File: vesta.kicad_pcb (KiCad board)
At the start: 2 copper layers, 39 parts, among them J1 Solar Panel, J2 Solar Panel, J4 Conn_02x07_Odd_Even, U2 BQ24074RGTR, U3 TPS63900DSKR, U4 BME688_C3664478, U5 RAK3172-T-8-SM-I

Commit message: feat: PCB design ready
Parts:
- added G***: LOGO, Logo:logo, F.Cu at (54.3, 77.0)
- moved BATTERY1 56.7 mm to (44.5, 22.7), turned to 180 degrees
- moved U4 55.2 mm to (44.9, 78.8)
- moved C22 54.8 mm to (42.2, 77.2)
- moved C23 54.7 mm to (42.2, 79.2)
- moved J1 44.7 mm to (53.0, 30.7), turned to 180 degrees
- moved J2 42.7 mm to (36.5, 30.7), turned to 180 degrees
- moved R16 39.8 mm to (57.8, 68.0), turned to 90 degrees
- moved R15 39.1 mm to (56.2, 68.0), turned to 90 degrees
- moved TP2 37.1 mm to (60.5, 67.0), turned to 180 degrees
- moved D1 35.6 mm to (47.0, 33.5), turned to -90 degrees
- moved C2 33.1 mm to (42.5, 34.5), turned to -90 degrees
- moved C1 33.0 mm to (44.5, 34.5), turned to -90 degrees
- moved TP1 32.7 mm to (56.8, 43.0), turned to 180 degrees
- moved TP3 30.0 mm to (35.2, 61.2)
- moved R11 29.5 mm to (35.2, 63.2)
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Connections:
- U5 pad 2: unconnected-(U5-PA2/UART2_TX-Pad2) -> /UART_TX
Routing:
- net /3V3_SYS: track 5.55 -> 106.5 mm
- net /I2C1_SCL: track 0.00 -> 55.6 mm, vias 0 -> 1
- net /I2C1_SDA: track 0.00 -> 53.2 mm, vias 0 -> 1
- net /VIN_SOLAR: track 0.00 -> 43.9 mm, vias 0 -> 1
- net /NRST: track 0.00 -> 31.5 mm, vias 0 -> 2
- net /BAT_RAW: track 0.00 -> 28.2 mm
- net /SYS_RAW: track 0.00 -> 28.1 mm, vias 0 -> 2
- net GND: track 0.00 -> 26.2 mm, vias 0 -> 4
- net /EXP_SPI_CS0: track 0.00 -> 25.1 mm, vias 0 -> 1
- net /SWO: track 0.00 -> 24.6 mm, vias 0 -> 2
- net /EXP_GPIO_CS1: track 0.00 -> 20.5 mm
- net /SPI1_MOSI: track 0.00 -> 20.0 mm
- net /SPI1_MISO: track 0.00 -> 18.0 mm
- net /EXP_INT_WAKE: track 0.00 -> 16.4 mm, vias 0 -> 1
- net /SPI1_SCK: track 0.00 -> 16.1 mm
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- added copper zone on B.Cu, net GND
- added copper zone on F.Cu, net GND
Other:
- board outline added: 41 x 60.2 mm
- board text added: "()()()()() ()()()()()()() ()()()()()()()()() ()()()()()()()()() ()()()()()()()()()()() ()()()()()()()()()()() ()()()()()()()()()()()() ()()()()()()()()()()()()() ()()()()()()()()()()()()()() ()()()()()()()()()()()()()()() ()()()()()()()()()()()()()()()() ()()()()()()()()()()()()()()()()() ()()()()()()()()()()()()()()()()() ()()()()()()()()()()()()()()()()() ()()()()()()()()()()()()()()()()() ()()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"
- board text added: "3V3"
- board text added: "EXP GPIO CS1"
- board text added: "EXP SPI CS0"
- board text added: "EXP_INT WAKE"
- board text added: "GND"
- board text added: "I2C1 SCL"
- board text added: "I2C1 SDA"
- board text added: "SPI1 MISO"
- board text added: "SPI1 MOSI"
- board text added: "SPI1 SCK"
- board text added: "Vesta Golden Marina Industries"
- board text removed: "()()() ()()()()() ()()()()()()() ()()()()()()()() ()()()()()()()()()()() ()()()()()()()()()()() ()()()()()()()()()()()() ()()()()()()()()()()()()() ()()()()()()()()()()()()()() ()()()()()()()()()()()()()()() ()()()()()()()()()()()()()()()() ()()()()()()()()()()()()()()()()() ()()()()()()()()()()()()()()()()() ()()()()()()()()()()()()()()()()() ()()()()()()()()()()()()()()()()() ()()()()()()()()()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"

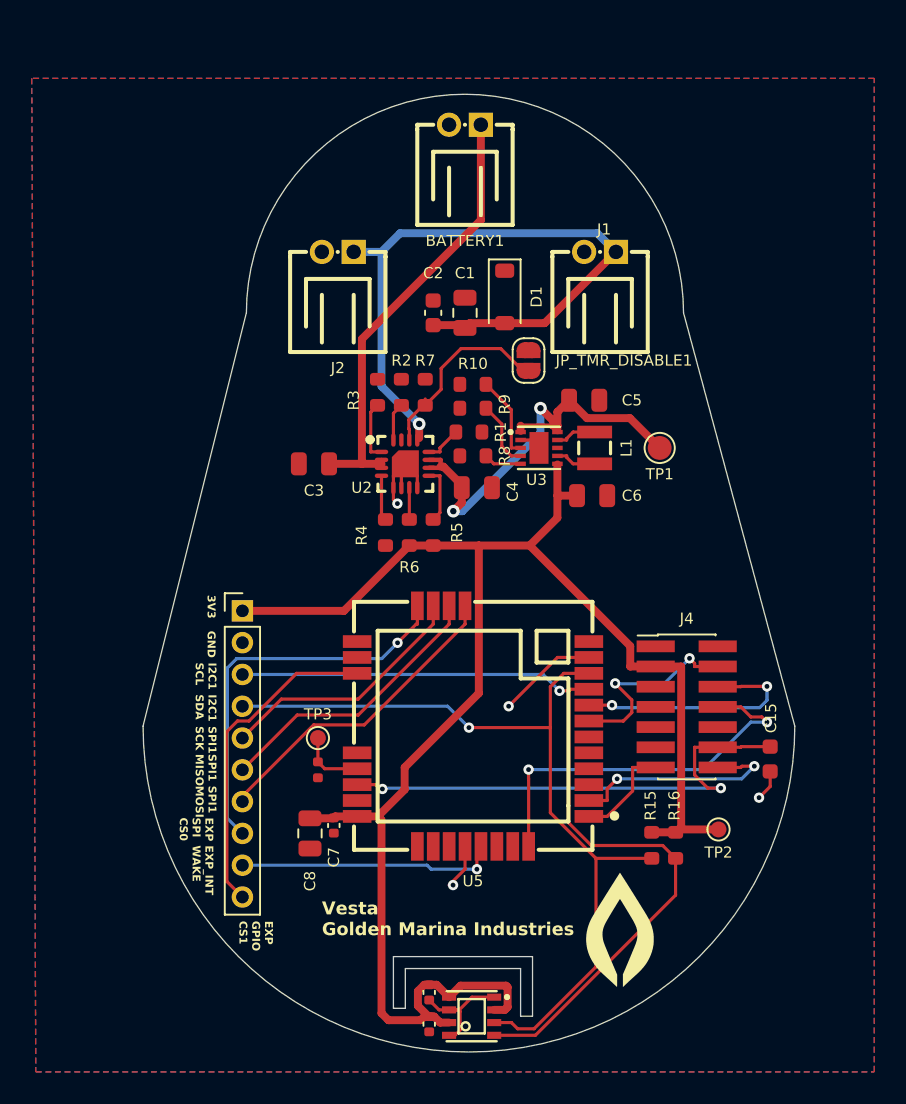
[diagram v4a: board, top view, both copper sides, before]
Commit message: feat: updaing the BOM and adding the STLINK connector
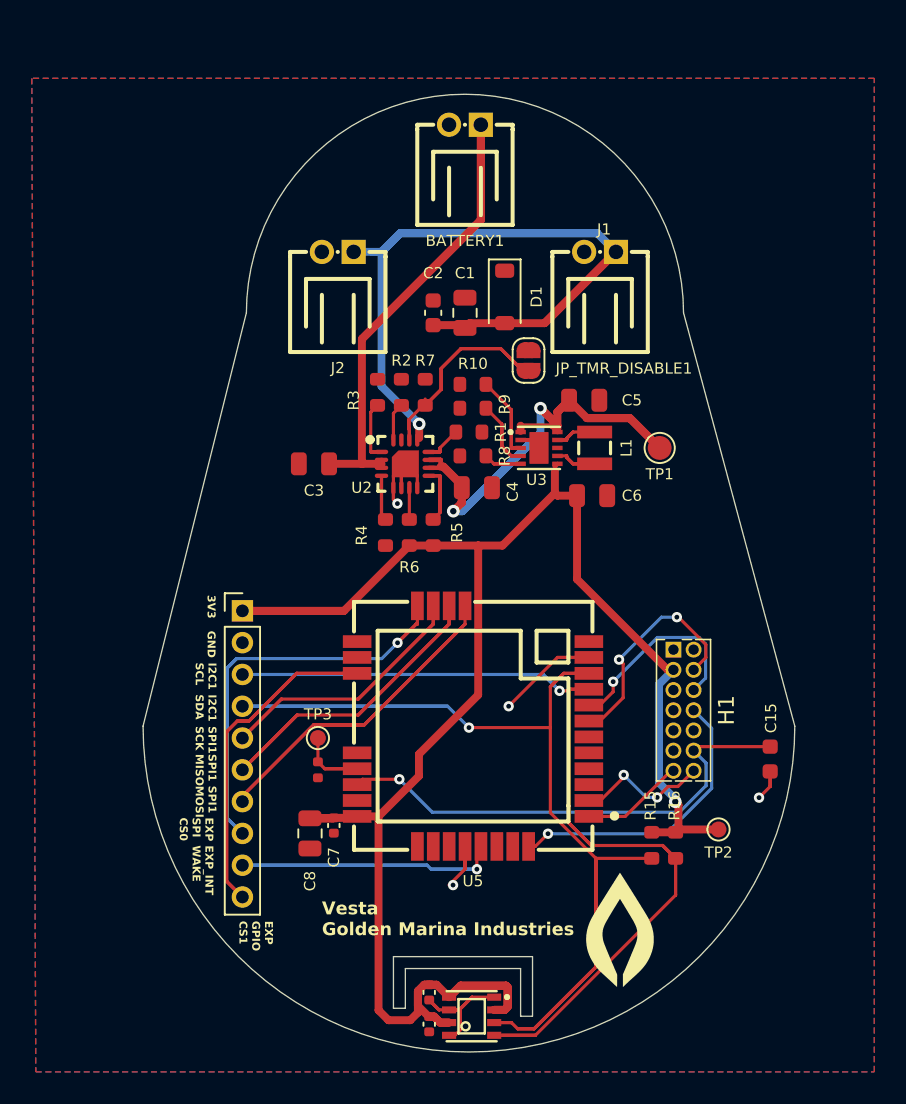
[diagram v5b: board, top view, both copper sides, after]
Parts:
- removed J4: Conn_02x07_Odd_Even, Connector_PinHeader_1.27mm:PinHeader_2x07_P1.27mm_Vertical_SMD
- added H1: HX_PZ1_27-2X7P_ZZ, JLCImport:HX_PZ1_27-2X7P_ZZ, F.Cu at (58.2, 59.5)
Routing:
- net /I2C1_SDA: track 53.2 -> 83.3 mm
- net /VIN_SOLAR: track 43.9 -> 65.5 mm
- net /I2C1_SCL: track 55.6 -> 74.6 mm
- net /SPI1_MOSI: track 20.0 -> 38.8 mm
- net /SYS_RAW: track 28.1 -> 46.7 mm
- net /3V3_SYS: track 106.5 -> 123.7 mm, vias 0 -> 1
- net /BAT_RAW: track 28.2 -> 44.8 mm
- net /EXP_INT_WAKE: track 16.4 -> 30.9 mm
- net GND: track 26.2 -> 40.6 mm
- net /SPI1_MISO: track 18.0 -> 32.1 mm
- net /EXP_SPI_CS0: track 25.1 -> 38.4 mm
- net /SPI1_SCK: track 16.1 -> 27.4 mm
- net /EXP_GPIO_CS1: track 20.5 -> 31.6 mm
- net Net-(JP_TMR_DISABLE1-A): track 12.4 -> 22.8 mm
- net /SWO: track 24.6 -> 18.4 mm, vias 2 -> 1
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
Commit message: feat: small improvements for second revision
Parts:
- C15: footprint PCM_JLCPCB:C_0603 -> Capacitor_SMD:C_0402_1005Metric
- moved C15 28.2 mm to (35.5, 62.8), turned to 90 degrees
- moved TMR_DIS 12.2 mm to (36.5, 39.8), turned to -90 degrees
- moved BATTERY1 8.16 mm to (44.5, 30.8), turned to 0 degrees
- moved J2 5.75 mm to (37.5, 36.3), turned to 0 degrees
- moved J1 5.67 mm to (52.8, 36.3), turned to 0 degrees
- moved C22 2.00 mm to (42.2, 79.2), turned to 90 degrees
- moved C23 2.00 mm to (42.2, 77.2), turned to 90 degrees
- moved C8 1.75 mm to (34.8, 65.5), turned to -90 degrees
- moved C3 1.50 mm to (36.5, 44.0)
- moved TP3 1.41 mm to (36.2, 60.2)
- moved R11 1.06 mm to (34.5, 62.5)
- moved C7 1.00 mm to (36.2, 65.8), turned to -90 degrees
- moved D1 0.56 mm to (47.5, 33.8)
- moved R2 0.18 mm to (40.5, 39.7)
- moved R3 0.18 mm to (39.0, 39.7)
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- renumbered JP_TMR_DISABLE1 to TMR_DIS
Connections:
- net /BAT_RAW renamed BAT_RAW
- net /SYS_RAW renamed SYS_RAW
- net /VIN_SOLAR renamed VIN_SOLAR
- C22 pad 1: /3V3_SYS -> GND
- C22 pad 2: GND -> 3V3_SYS
- C23 pad 1: /3V3_SYS -> GND
- C23 pad 2: GND -> 3V3_SYS
- C6 pad 2: /3V3_SYS -> 3V3_SYS
- C7 pad 2: /3V3_SYS -> 3V3_SYS
- C8 pad 2: /3V3_SYS -> 3V3_SYS
- H1 pad 3: /3V3_SYS -> 3V3_SYS
- J_EXP1 pad 1: /3V3_SYS -> 3V3_SYS
- R15 pad 1: /I2C1_SDA -> 3V3_SYS
- R15 pad 2: /3V3_SYS -> /I2C1_SDA
- R16 pad 1: /I2C1_SCL -> 3V3_SYS
- R16 pad 2: /3V3_SYS -> /I2C1_SCL
- R5 pad 1: /3V3_SYS -> /CHARGER_CHG_N
- R5 pad 2: /CHARGER_CHG_N -> 3V3_SYS
- R6 pad 1: /3V3_SYS -> 3V3_SYS
- TP2 pad 1: /3V3_SYS -> 3V3_SYS
- U3 pad 6: /3V3_SYS -> 3V3_SYS
- U4 pad 2: /3V3_SYS -> 3V3_SYS
- U4 pad 6: /3V3_SYS -> 3V3_SYS
- U4 pad 8: /3V3_SYS -> 3V3_SYS
- U5 pad 24: /3V3_SYS -> 3V3_SYS
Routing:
- net /3V3_SYS: track 123.7 -> 0.00 mm, vias 1 -> 0
- net GND: track 40.6 -> 102.3 mm, vias 4 -> 9
- net VIN_SOLAR: track 65.5 -> 25.0 mm, vias 1 -> 0
- net /I2C1_SDA: track 83.3 -> 52.9 mm
- net /I2C1_SCL: track 74.6 -> 54.6 mm, vias 1 -> 3
- net 3V3_SYS: track 0.00 -> 18.4 mm, vias 0 -> 4
- net /EXP_SPI_CS0: track 38.4 -> 20.8 mm, vias 1 -> 0
- net BAT_RAW: track 44.8 -> 28.7 mm
- net /EXP_INT_WAKE: track 30.9 -> 16.1 mm, vias 1 -> 0
- net Net-(JP_TMR_DISABLE1-A): track 22.8 -> 8.67 mm
- net /EXP_GPIO_CS1: track 31.6 -> 18.3 mm
- net SYS_RAW: track 46.7 -> 33.6 mm, vias 2 -> 0
- net /SPI1_MOSI: track 38.8 -> 26.6 mm, vias 0 -> 2
- net /SPI1_MISO: track 32.1 -> 21.4 mm
- net /SPI1_SCK: track 27.4 -> 18.6 mm, vias 0 -> 1
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- added copper zone on B.Cu, net 3V3_SYS
- added copper zone on F.Cu, net 3V3_SYS
- added copper zone on In1.Cu, net GND
- added copper zone on In2.Cu, net GND
- removed copper zone on B.Cu, net GND
- removed copper zone on F.Cu, net GND
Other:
- outline, holes or cut-outs redrawn
- copper layers 2 -> 4
